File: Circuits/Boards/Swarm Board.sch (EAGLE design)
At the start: 95 parts, among them CON1 ISP(2X3), T1 NPN2N2222, T10 TEFT4300, T11 NPN2N2222, T12 NPN2N2222, T13 NPN2N2222, T14 NPN2N2222, T15 NPN2N2222, T16 NPN2N2222, T17 NPN2N2222, T18 NPN2N2222, T2 NPN2N2222, T3 NPN2N2222, T4 TEFT4300, T5 TEFT4300, T6 TEFT4300, T7 TEFT4300, T8 TEFT4300, T9 TEFT4300, U1 ATMEGA324P, U2 MCP73832SOT-23, U3 TB6552FN/FNG

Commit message: 
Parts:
- removed R29, R31: 10k, Passive:RES0603
- removed R30, R32: 1k, Passive:RES0603
- removed T11, T12: NPN2N2222, Passive:NPN2N2222
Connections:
- removed net AIN: R30.1, U1.PB0(XCK0/T0/PCINT8), U3.AIN1
- removed net BIN: R32.1, U1.PB2(AIN0/INT2/PCINT10), U3.BIN1
- removed net N$22: R30.2, T11.B
- removed net N$28: R36.1, T13.C
- removed net N$29: R37.1, T14.C
- removed net N$30: R38.1, T15.C
- removed net N$31: R39.1, T16.C
- removed net N$32: R40.1, T17.C
- removed net N$33: R41.1, T18.C
- removed net N$7: R32.2, T12.B
- new net AIN1: U1.PD2(PCINT26/RXD1/INT0), U3.AIN1
- new net BIN1: U1.PD5(PCINT29/OC1A), U3.BIN1
- new net RX1: R36.1, T13.C, U1.PC2(PCINT18/TCK)
- new net RX2: R37.1, T14.C, U1.PC3(PCINT19/TMS)
- new net RX3: R38.1, T15.C, U1.PC4(TDO/PCINT20)
- new net RX4: R39.1, T16.C, U1.PC5(TDI/PCINT21)
- new net RX5: R40.1, T17.C, U1.PC6(TOSC1/PCINT22)
- new net RX6: R41.1, T18.C, U1.PC7(TOSC2/PCINT23)
- net +3V: no longer LED8.A, LED9.A, R29.1, R31.1, U$1.+3V
- net +VBAT: now also U$1.7; no longer U$1.BAT+
- net AIN2: now also U1.PD3(PCINT27/TXD1/INT1); no longer R29.2, T11.C
- net APWM: now also U1.PD6(PCINT30/OC2B/ICP); no longer U1.PB3(AIN1/OC0A/PCINT11)
- net BIN2: now also U1.PD4(PCINT28/XCK1/OC1B); no longer R31.2, T12.C
- net BPWM: now also U1.PD7(PCINT31/OC2A); no longer U1.PB4(!SS!/OC0B/PCINT12)
- net BUMPER: now also U1.PA3(ADC3/PCINT3); no longer U$1.BUMP, U1.PA2(ADC2/PCINT2)
- net BUZZER: now also U1.PB4(!SS!/OC0B/PCINT12)
- net CHGDETECT: now also U1.PB0(XCK0/T0/PCINT8)
- net CHGSTATUS: now also U1.PB1(T1/CLKO/PCINT9)
- net DISTANCELED: now also U1.PA6(ADC6/PCINT6); no longer U1.PA5(ADC5/PCINT5)
- net DISTANCERECEIVE: now also U1.PA7(ADC7/PCINT7); no longer U1.PA6(ADC6/PCINT6)
- net GND: now also R25.1, R26.1, U$1.6, U$1.8; no longer T11.E, T12.E, U$1.BAT-, U$1.GND
- net IRENABLE: now also U$1.9, U1.PA4(ADC4/PCINT4); no longer U$1.ENABLE, U1.PA3(ADC3/PCINT3)
- net LED1: now also LED8.A, U1.PB2(AIN0/INT2/PCINT10); no longer R25.1
- net LED2: now also LED9.A, U1.PB3(AIN1/OC0A/PCINT11); no longer R26.1
- net LIGHTSENSE: now also U1.PA5(ADC5/PCINT5); no longer U1.PA4(ADC4/PCINT4)
- net LINESENSE1: now also U1.PA1(ADC1/PCINT1); no longer U$1.LINER, U1.PA0(ADC0/PCINT0)
- net LINESENSE2: now also U1.PA2(ADC2/PCINT2); no longer U$1.LINEL, U1.PA1(ADC1/PCINT1)
- net MA+: now also U$1.12; no longer U$1.MA+
- net MA-: now also U$1.11; no longer U$1.MA-
- net MB+: now also U$1.2; no longer U$1.MB+
- net MB-: now also U$1.1; no longer U$1.MB-
- net STBY: now also U1.PC0(PCINT16/SCL); no longer U1.PB1(T1/CLKO/PCINT9)
- net TRANSMITLEDS: now also U1.PC1(PCINT17/SDA)
- net VSENSE: now also U1.PA0(ADC0/PCINT0); no longer U1.PA7(ADC7/PCINT7)
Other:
- moved on the sheet: R33, R34, R35, U$2

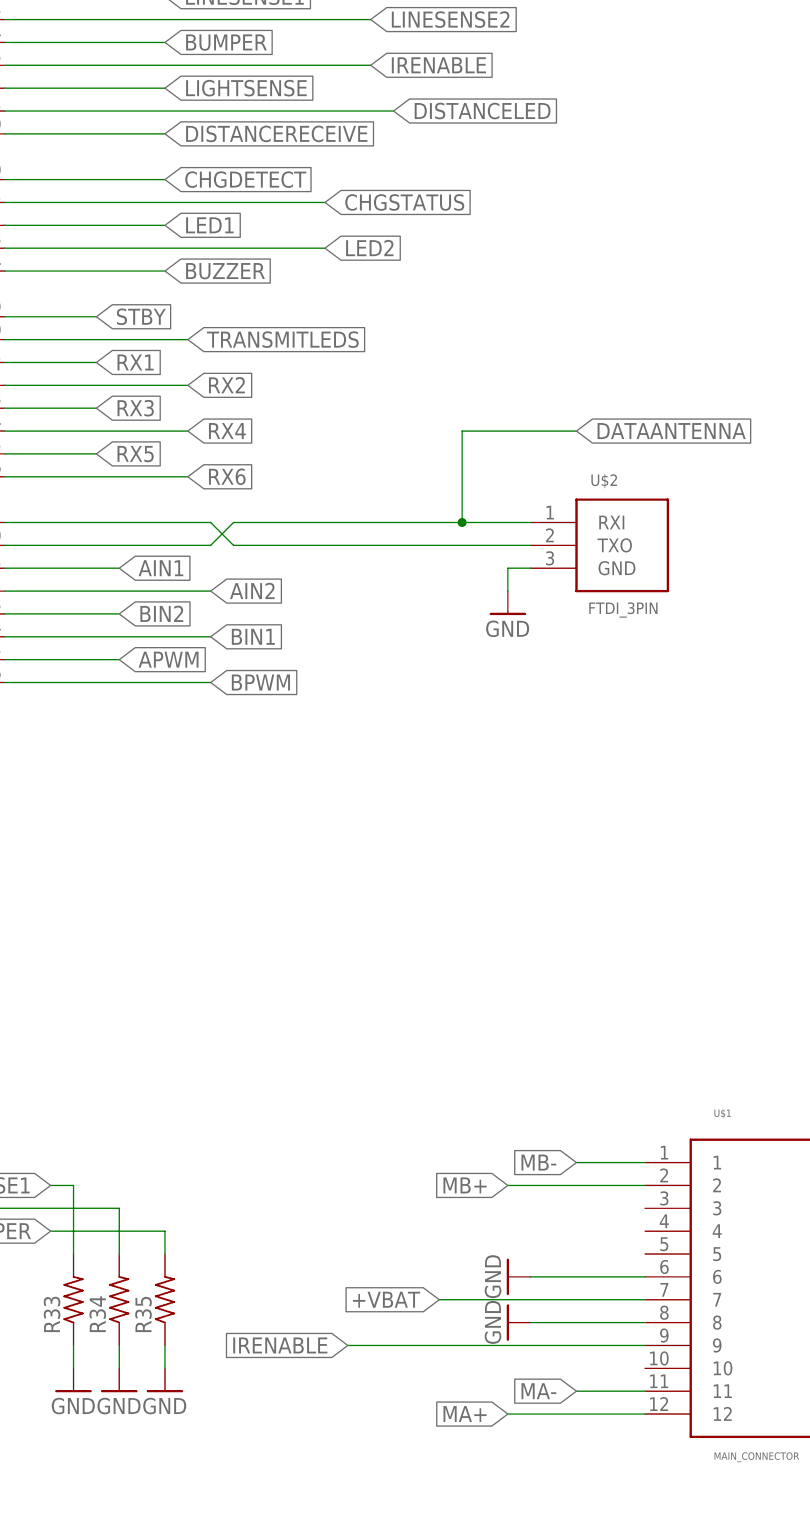
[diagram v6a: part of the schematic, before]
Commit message: 
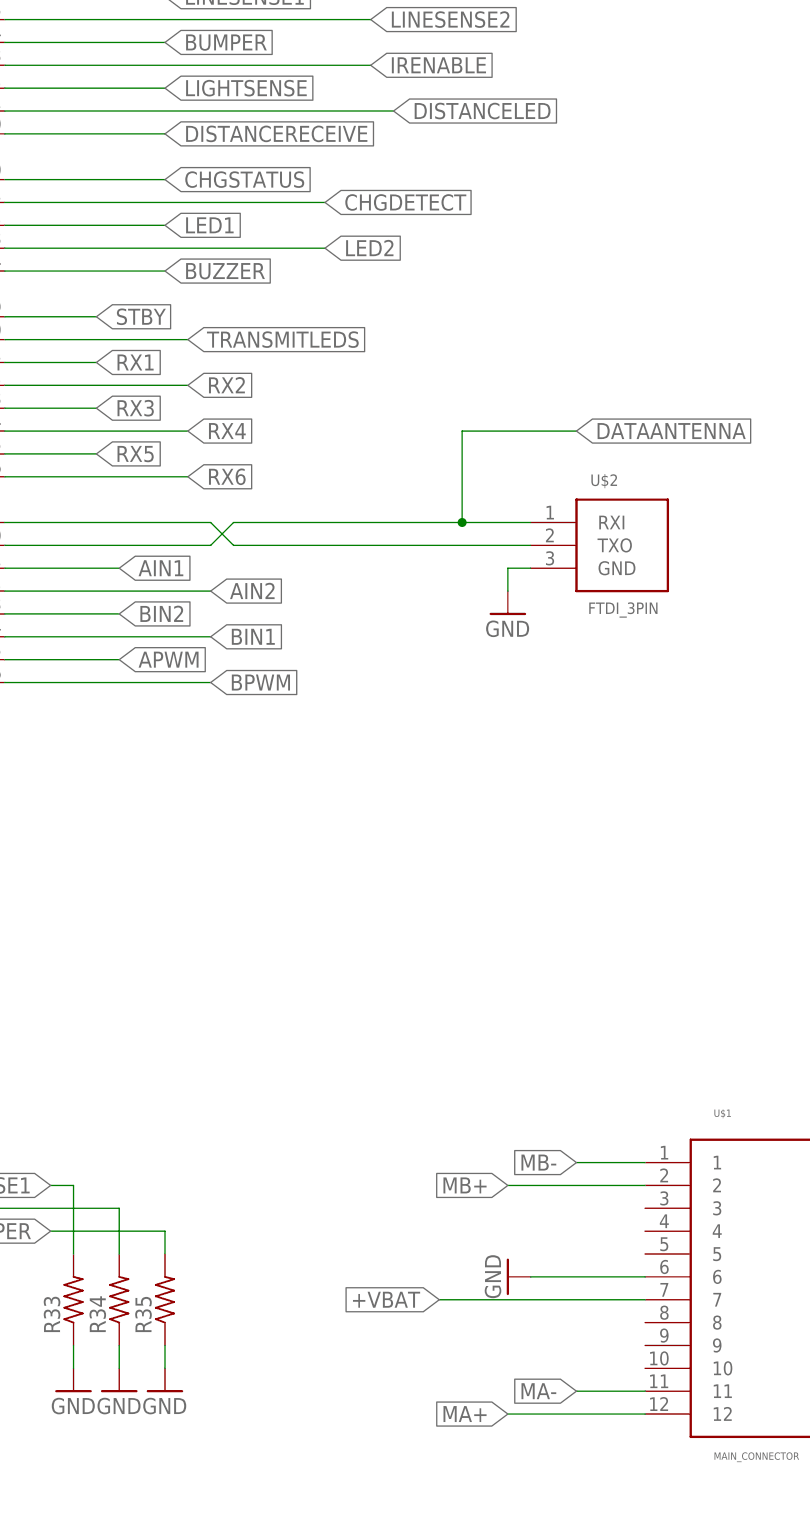
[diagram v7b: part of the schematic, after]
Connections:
- net CHGDETECT: now also U1.PB1(T1/CLKO/PCINT9); no longer U1.PB0(XCK0/T0/PCINT8)
- net CHGSTATUS: now also U1.PB0(XCK0/T0/PCINT8); no longer U1.PB1(T1/CLKO/PCINT9)
- net GND: no longer U$1.8
- net IRENABLE: no longer U$1.9
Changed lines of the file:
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@@
 <part name="GND19" library="Supply" deviceset="GND" device=""/>
 <part name="P+17" library="Supply" deviceset="+3V" device=""/>
-<part name="GND20" library="Supply" deviceset="GND" device=""/>
 <part name="R33" library="Passive" deviceset="RES" device="0603"/>
 <part name="R34" library="Passive" deviceset="RES" device="0603"/>
@@
 <instance part="GND19" gate="1" x="266.7" y="-40.64"/>
 <instance part="P+17" gate="1" x="266.7" y="2.54"/>
-<instance part="GND20" gate="1" x="86.36" y="-111.76" rot="R270"/>
 <instance part="R33" gate="G$1" x="38.1" y="-109.22" rot="R90"/>
 <instance part="R34" gate="G$1" x="43.18" y="-109.22" rot="R90"/>
@@
 </segment>
 <segment>
-<pinref part="U$1" gate="G$1" pin="8"/>
-<wire x1="101.6" y1="-111.76" x2="88.9" y2="-111.76" width="0.1524" layer="91"/>
-<pinref part="GND20" gate="1" pin="GND"/>
-</segment>
-<segment>
 <pinref part="R33" gate="G$1" pin="1"/>
 <wire x1="38.1" y1="-114.3" x2="38.1" y2="-116.84" width="0.1524" layer="91"/>
@@
 </segment>
 <segment>
-<pinref part="U1" gate="G$1" pin="PB0(XCK0/T0/PCINT8)"/>
-<wire x1="30.48" y1="15.24" x2="48.26" y2="15.24" width="0.1524" layer="91"/>
-<label x="48.26" y="15.24" size="1.778" layer="91" xref="yes"/>
+<pinref part="U1" gate="G$1" pin="PB1(T1/CLKO/PCINT9)"/>
+<wire x1="30.48" y1="12.7" x2="66.04" y2="12.7" width="0.1524" layer="91"/>
+<label x="66.04" y="12.7" size="1.778" layer="91" xref="yes"/>
 </segment>
 </net>
@@
 </segment>
 <segment>
-<pinref part="U1" gate="G$1" pin="PB1(T1/CLKO/PCINT9)"/>
-<wire x1="30.48" y1="12.7" x2="66.04" y2="12.7" width="0.1524" layer="91"/>
-<label x="66.04" y="12.7" size="1.778" layer="91" xref="yes"/>
+<pinref part="U1" gate="G$1" pin="PB0(XCK0/T0/PCINT8)"/>
+<wire x1="30.48" y1="15.24" x2="48.26" y2="15.24" width="0.1524" layer="91"/>
+<label x="48.26" y="15.24" size="1.778" layer="91" xref="yes"/>
 </segment>
 </net>
@@
 <net name="IRENABLE" class="0">
 <segment>
-<pinref part="U$1" gate="G$1" pin="9"/>
-<wire x1="101.6" y1="-114.3" x2="68.58" y2="-114.3" width="0.1524" layer="91"/>
-<label x="68.58" y="-114.3" size="1.778" layer="91" rot="R180" xref="yes"/>
-</segment>
-<segment>
 <pinref part="U1" gate="G$1" pin="PA4(ADC4/PCINT4)"/>

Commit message: Finished routing
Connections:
- net +3V: now also U$1.8
- net BUMPER: now also U$1.5
- net GND: now also U$1.9
- net IRENABLE: now also U$1.10
- net LINESENSE1: now also U$1.3
- net LINESENSE2: now also U$1.4
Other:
- moved on the sheet: R33, R34, R35
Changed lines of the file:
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@@
 <part name="GND28" library="Supply" deviceset="GND" device=""/>
 <part name="GND21" library="Supply" deviceset="GND" device=""/>
+<part name="GND20" library="Supply" deviceset="GND" device=""/>
+<part name="P+3" library="Supply" deviceset="+3V" device=""/>
 </parts>
 <sheets>
@@
 <instance part="GND19" gate="1" x="266.7" y="-40.64"/>
 <instance part="P+17" gate="1" x="266.7" y="2.54"/>
-<instance part="R33" gate="G$1" x="38.1" y="-109.22" rot="R90"/>
-<instance part="R34" gate="G$1" x="43.18" y="-109.22" rot="R90"/>
-<instance part="R35" gate="G$1" x="48.26" y="-109.22" rot="R90"/>
-<instance part="GND23" gate="1" x="38.1" y="-119.38"/>
-<instance part="GND24" gate="1" x="43.18" y="-119.38"/>
-<instance part="GND25" gate="1" x="48.26" y="-119.38"/>
+<instance part="R33" gate="G$1" x="50.8" y="-111.76" rot="R90"/>
+<instance part="R34" gate="G$1" x="55.88" y="-111.76" rot="R90"/>
+<instance part="R35" gate="G$1" x="60.96" y="-111.76" rot="R90"/>
+<instance part="GND23" gate="1" x="50.8" y="-121.92"/>
+<instance part="GND24" gate="1" x="55.88" y="-121.92"/>
+<instance part="GND25" gate="1" x="60.96" y="-121.92"/>
 <instance part="GND26" gate="1" x="-48.26" y="81.28" rot="R90"/>
 <instance part="P+21" gate="G$1" x="-50.8" y="101.6" rot="R270"/>
@@
 <instance part="R40" gate="G$1" x="381" y="96.52" rot="R90"/>
 <instance part="R41" gate="G$1" x="401.32" y="96.52" rot="R90"/>
-<instance part="GND28" gate="1" x="86.36" y="-106.68" rot="R270"/>
+<instance part="GND28" gate="1" x="78.74" y="-106.68" rot="R270"/>
 <instance part="GND21" gate="1" x="-165.1" y="-48.26"/>
+<instance part="GND20" gate="1" x="96.52" y="-114.3" rot="R270"/>
+<instance part="P+3" gate="1" x="88.9" y="-111.76" rot="R90"/>
 </instances>
 <busses>
@@
 <pinref part="P+17" gate="1" pin="+3V"/>
 </segment>
+<segment>
+<pinref part="U$1" gate="G$1" pin="8"/>
+<wire x1="101.6" y1="-111.76" x2="91.44" y2="-111.76" width="0.1524" layer="91"/>
+<pinref part="P+3" gate="1" pin="+3V"/>
+</segment>
 </net>
 <net name="GND" class="0">
@@
 <segment>
 <pinref part="U$1" gate="G$1" pin="6"/>
-<wire x1="101.6" y1="-106.68" x2="88.9" y2="-106.68" width="0.1524" layer="91"/>
+<wire x1="101.6" y1="-106.68" x2="81.28" y2="-106.68" width="0.1524" layer="91"/>
 <pinref part="GND28" gate="1" pin="GND"/>
 </segment>
@@
 <segment>
 <pinref part="R33" gate="G$1" pin="1"/>
-<wire x1="38.1" y1="-114.3" x2="38.1" y2="-116.84" width="0.1524" layer="91"/>
+<wire x1="50.8" y1="-116.84" x2="50.8" y2="-119.38" width="0.1524" layer="91"/>
 <pinref part="GND23" gate="1" pin="GND"/>
 </segment>
 <segment>
 <pinref part="R34" gate="G$1" pin="1"/>
-<wire x1="43.18" y1="-114.3" x2="43.18" y2="-116.84" width="0.1524" layer="91"/>
+<wire x1="55.88" y1="-116.84" x2="55.88" y2="-119.38" width="0.1524" layer="91"/>
 <pinref part="GND24" gate="1" pin="GND"/>
 </segment>
 <segment>
 <pinref part="R35" gate="G$1" pin="1"/>
-<wire x1="48.26" y1="-114.3" x2="48.26" y2="-116.84" width="0.1524" layer="91"/>
+<wire x1="60.96" y1="-116.84" x2="60.96" y2="-119.38" width="0.1524" layer="91"/>
 <pinref part="GND25" gate="1" pin="GND"/>
 </segment>
@@
 <wire x1="-165.1" y1="-43.18" x2="-165.1" y2="-45.72" width="0.1524" layer="91"/>
 <pinref part="GND21" gate="1" pin="GND"/>
+</segment>
+<segment>
+<pinref part="U$1" gate="G$1" pin="9"/>
+<wire x1="101.6" y1="-114.3" x2="99.06" y2="-114.3" width="0.1524" layer="91"/>
+<pinref part="GND20" gate="1" pin="GND"/>
 </segment>
 </net>
@@
 <segment>
 <pinref part="U$1" gate="G$1" pin="7"/>
-<wire x1="101.6" y1="-109.22" x2="78.74" y2="-109.22" width="0.1524" layer="91"/>
-<label x="78.74" y="-109.22" size="1.778" layer="91" rot="R180" xref="yes"/>
+<wire x1="101.6" y1="-109.22" x2="76.2" y2="-109.22" width="0.1524" layer="91"/>
+<label x="76.2" y="-109.22" size="1.778" layer="91" rot="R180" xref="yes"/>
 </segment>
 </net>
@@
 <net name="LINESENSE1" class="0">
 <segment>
-<label x="35.56" y="-96.52" size="1.778" layer="91" rot="R180" xref="yes"/>
-<wire x1="38.1" y1="-96.52" x2="35.56" y2="-96.52" width="0.1524" layer="91"/>
-<wire x1="38.1" y1="-96.52" x2="38.1" y2="-104.14" width="0.1524" layer="91"/>
-<pinref part="R33" gate="G$1" pin="2"/>
-</segment>
-<segment>
 <pinref part="U1" gate="G$1" pin="PA1(ADC1/PCINT1)"/>
 <wire x1="30.48" y1="35.56" x2="48.26" y2="35.56" width="0.1524" layer="91"/>
 <label x="48.26" y="35.56" size="1.778" layer="91" xref="yes"/>
 </segment>
+<segment>
+<pinref part="U$1" gate="G$1" pin="3"/>
+<label x="48.26" y="-99.06" size="1.778" layer="91" rot="R180" xref="yes"/>
+<wire x1="50.8" y1="-99.06" x2="48.26" y2="-99.06" width="0.1524" layer="91"/>
+<wire x1="50.8" y1="-99.06" x2="50.8" y2="-106.68" width="0.1524" layer="91"/>
+<pinref part="R33" gate="G$1" pin="2"/>
+<wire x1="101.6" y1="-99.06" x2="50.8" y2="-99.06" width="0.1524" layer="91"/>
+<junction x="50.8" y="-99.06"/>
+</segment>
 </net>
 <net name="LINESENSE2" class="0">
-<segment>
-<label x="17.78" y="-99.06" size="1.778" layer="91" rot="R180" xref="yes"/>
-<wire x1="43.18" y1="-99.06" x2="17.78" y2="-99.06" width="0.1524" layer="91"/>
-<wire x1="43.18" y1="-99.06" x2="43.18" y2="-104.14" width="0.1524" layer="91"/>
-<pinref part="R34" gate="G$1" pin="2"/>
-</segment>
 <segment>
 <pinref part="U1" gate="G$1" pin="PA2(ADC2/PCINT2)"/>
 <wire x1="30.48" y1="33.02" x2="71.12" y2="33.02" width="0.1524" layer="91"/>
 <label x="71.12" y="33.02" size="1.778" layer="91" xref="yes"/>
+</segment>
+<segment>
+<pinref part="U$1" gate="G$1" pin="4"/>
+<label x="30.48" y="-101.6" size="1.778" layer="91" rot="R180" xref="yes"/>
+<wire x1="55.88" y1="-101.6" x2="53.34" y2="-101.6" width="0.1524" layer="91"/>
+<wire x1="53.34" y1="-101.6" x2="30.48" y2="-101.6" width="0.1524" layer="91"/>
+<wire x1="55.88" y1="-101.6" x2="55.88" y2="-106.68" width="0.1524" layer="91"/>
+<pinref part="R34" gate="G$1" pin="2"/>
+<wire x1="101.6" y1="-101.6" x2="55.88" y2="-101.6" width="0.1524" layer="91"/>
+<junction x="55.88" y="-101.6"/>
 </segment>
 </net>
@@
 <segment>
 <pinref part="U$1" gate="G$1" pin="11"/>
-<wire x1="101.6" y1="-119.38" x2="93.98" y2="-119.38" width="0.1524" layer="91"/>
-<label x="93.98" y="-119.38" size="1.778" layer="91" rot="R180" xref="yes"/>
+<wire x1="101.6" y1="-119.38" x2="78.74" y2="-119.38" width="0.1524" layer="91"/>
+<label x="78.74" y="-119.38" size="1.778" layer="91" rot="R180" xref="yes"/>
 </segment>
 </net>
@@
 <segment>
 <pinref part="U$1" gate="G$1" pin="2"/>
-<wire x1="101.6" y1="-96.52" x2="86.36" y2="-96.52" width="0.1524" layer="91"/>
-<label x="86.36" y="-96.52" size="1.778" layer="91" rot="R180" xref="yes"/>
+<wire x1="101.6" y1="-96.52" x2="76.2" y2="-96.52" width="0.1524" layer="91"/>
+<label x="76.2" y="-96.52" size="1.778" layer="91" rot="R180" xref="yes"/>
 </segment>
 </net>
@@
 <segment>
 <pinref part="U$1" gate="G$1" pin="1"/>
-<wire x1="101.6" y1="-93.98" x2="93.98" y2="-93.98" width="0.1524" layer="91"/>
-<label x="93.98" y="-93.98" size="1.778" layer="91" rot="R180" xref="yes"/>
+<wire x1="101.6" y1="-93.98" x2="83.82" y2="-93.98" width="0.1524" layer="91"/>
+<label x="83.82" y="-93.98" size="1.778" layer="91" rot="R180" xref="yes"/>
 </segment>
 </net>
@@
 <label x="71.12" y="27.94" size="1.778" layer="91" xref="yes"/>
 </segment>
+<segment>
+<pinref part="U$1" gate="G$1" pin="10"/>
+<wire x1="101.6" y1="-116.84" x2="93.98" y2="-116.84" width="0.1524" layer="91"/>
+<label x="93.98" y="-116.84" size="1.778" layer="91" rot="R180" xref="yes"/>
+</segment>
 </net>
 <net name="BUMPER" class="0">
-<segment>
-<label x="35.56" y="-101.6" size="1.778" layer="91" rot="R180" xref="yes"/>
-<wire x1="48.26" y1="-101.6" x2="35.56" y2="-101.6" width="0.1524" layer="91"/>
-<wire x1="48.26" y1="-101.6" x2="48.26" y2="-104.14" width="0.1524" layer="91"/>
-<pinref part="R35" gate="G$1" pin="2"/>
-</segment>
 <segment>
 <pinref part="U1" gate="G$1" pin="PA3(ADC3/PCINT3)"/>
@@
 <label x="48.26" y="30.48" size="1.778" layer="91" xref="yes"/>
 </segment>
-</net>
+<segment>
+<pinref part="U$1" gate="G$1" pin="5"/>
+<label x="48.26" y="-104.14" size="1.778" layer="91" rot="R180" xref="yes"/>
+<wire x1="60.96" y1="-104.14" x2="48.26" y2="-104.14" width="0.1524" layer="91"/>
+<wire x1="60.96" y1="-104.14" x2="60.96" y2="-106.68" width="0.1524" layer="91"/>
+<pinref part="R35" gate="G$1" pin="2"/>
+<wire x1="101.6" y1="-104.14" x2="60.96" y2="-104.14" width="0.1524" layer="91"/>
+<junction x="60.96" y="-104.14"/>
+</segment>
+</net>
